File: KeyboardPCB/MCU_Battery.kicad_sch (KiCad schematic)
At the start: 42 parts, among them Q1 CSD17527Q5A, Q2 CSD17527Q5A, U1 ATmega32U4-M, U2 TPS61236PRWLT, U3 BQ24193RGER, U4 BQ297xy, Y1 ECS-160-7-33B-CKL-TR

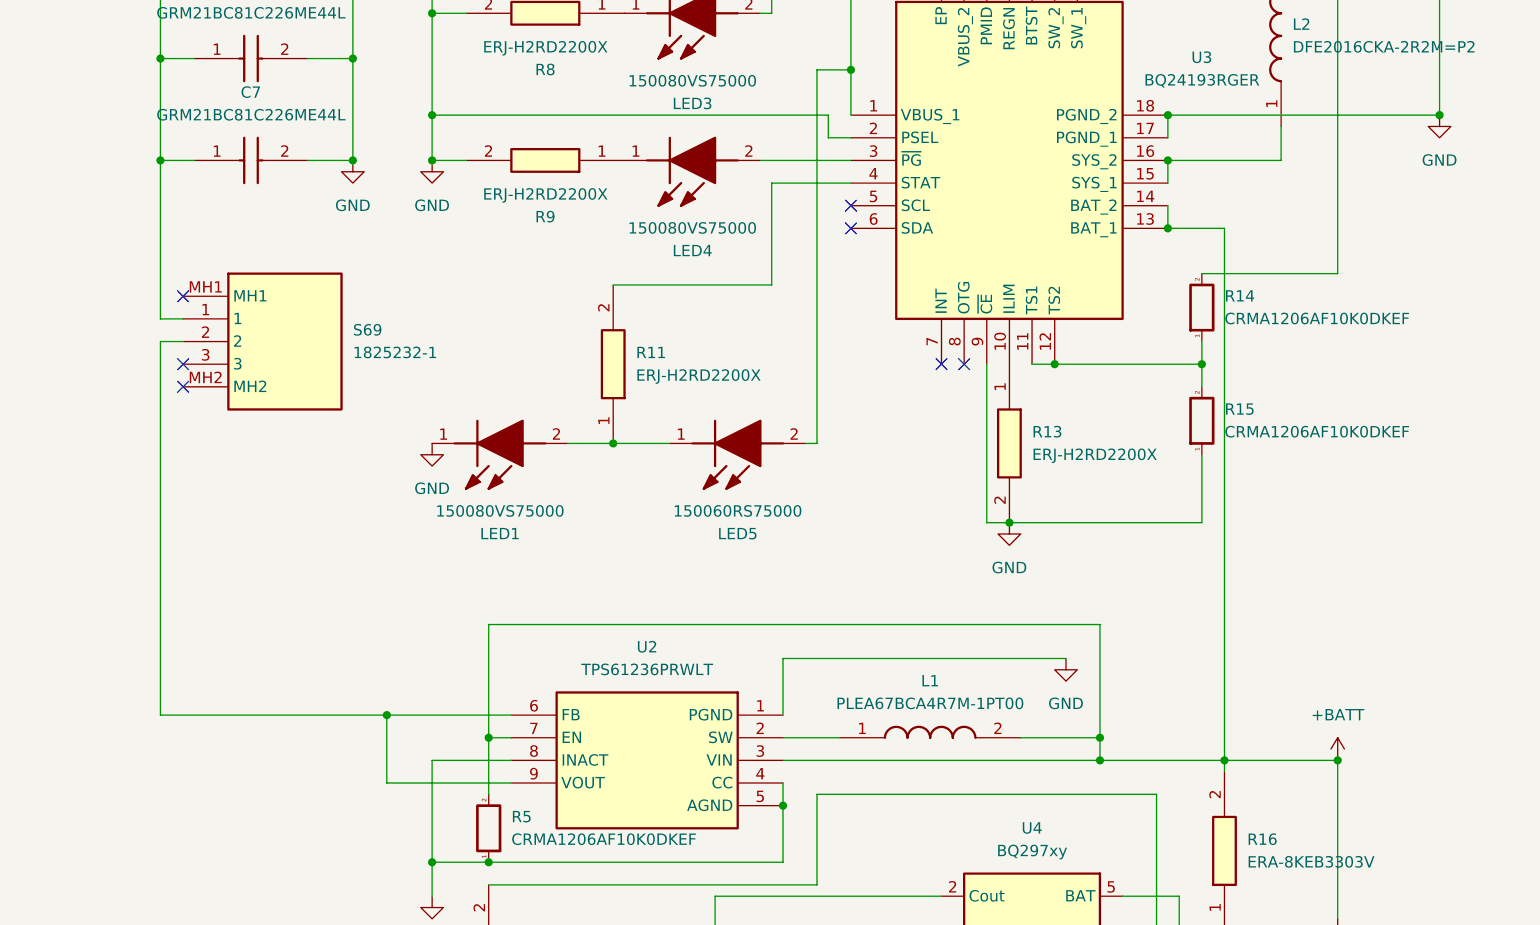
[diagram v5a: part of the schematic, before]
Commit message: Changed location of switch
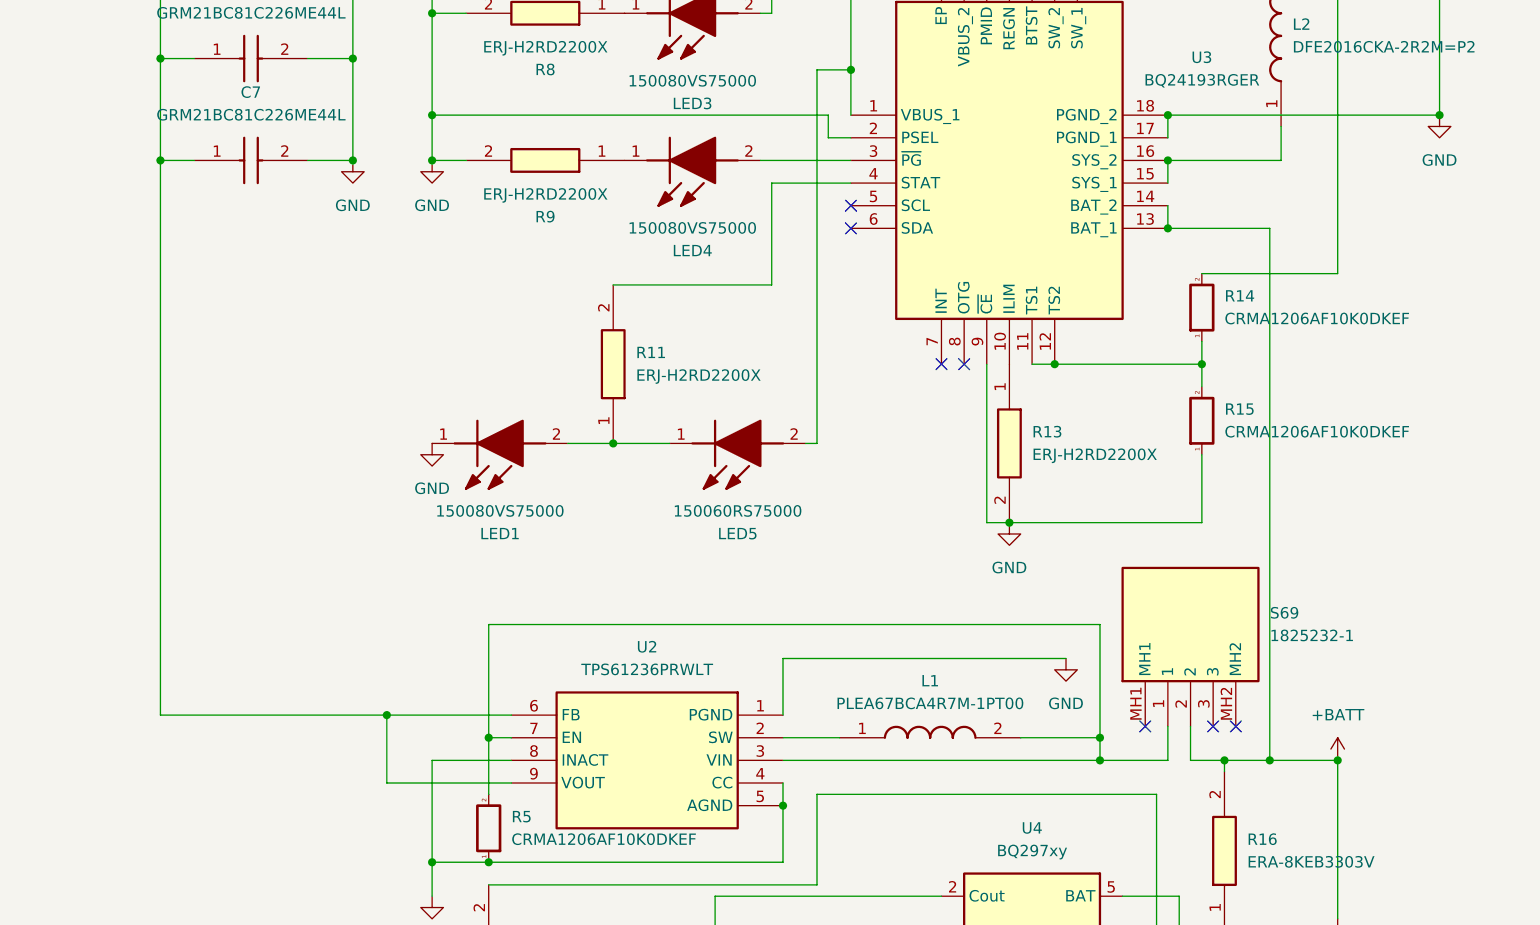
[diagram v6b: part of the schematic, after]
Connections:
- net +BATT: now also S69.2; no longer L1.2, R5.2, U2.3 (VIN), U2.7 (EN)
- net VBUSOUT: now also U2.6 (FB), U2.9 (VOUT); no longer S69.1
- new net: L1.2, R5.2, S69.1, U2.3 (VIN), U2.7 (EN)
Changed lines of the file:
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@@
   (junction (at 73.66 15.24) (diameter 0) (color 0 0 0 0)
   )
+  (junction (at 248.92 118.11) (diameter 0) (color 0 0 0 0)
+  )
+  (junction (at 254 118.11) (diameter 0) (color 0 0 0 0)
+  )
+  (junction (at 229.87 73.66) (diameter 0) (color 0 0 0 0)
+  )
+  (junction (at 160.02 45.72) (diameter 0) (color 0 0 0 0)
+  )
+  (junction (at 55.88 15.24) (diameter 0) (color 0 0 0 0)
+  )
+  (junction (at 166.37 115.57) (diameter 0) (color 0 0 0 0)
+  )
+  (junction (at 261.62 152.4) (diameter 0) (color 0 0 0 0)
+  )
+  (junction (at 160.02 50.8) (diameter 0) (color 0 0 0 0)
+  )
+  (junction (at 40.64 41.91) (diameter 0) (color 0 0 0 0)
+  )
+  (junction (at 250.19 20.32) (diameter 0) (color 0 0 0 0)
+  )
+  (junction (at 55.88 36.83) (diameter 0) (color 0 0 0 0)
+  )
+  (junction (at 242.57 45.72) (diameter 0) (color 0 0 0 0)
+  )
+  (junction (at 219.71 15.24) (diameter 0) (color 0 0 0 0)
+  )
+  (junction (at 255.27 152.4) (diameter 0) (color 0 0 0 0)
+  )
+  (junction (at 129.54 39.37) (diameter 0) (color 0 0 0 0)
+  )
+  (junction (at 261.62 118.11) (diameter 0) (color 0 0 0 0)
+  )
+  (junction (at 179.07 157.48) (diameter 0) (color 0 0 0 0)
+  )
+  (junction (at 217.17 138.43) (diameter 0) (color 0 0 0 0)
+  )
+  (junction (at 209.55 157.48) (diameter 0) (color 0 0 0 0)
+  )
+  (junction (at 248.92 139.7) (diameter 0) (color 0 0 0 0)
+  )
+  (junction (at 129.54 27.94) (diameter 0) (color 0 0 0 0)
+  )
   (junction (at 234.95 118.11) (diameter 0) (color 0 0 0 0)
   )
-  (junction (at 229.87 73.66) (diameter 0) (color 0 0 0 0)
-  )
-  (junction (at 160.02 45.72) (diameter 0) (color 0 0 0 0)
-  )
-  (junction (at 55.88 15.24) (diameter 0) (color 0 0 0 0)
-  )
-  (junction (at 166.37 115.57) (diameter 0) (color 0 0 0 0)
-  )
-  (junction (at 248.92 118.11) (diameter 0) (color 0 0 0 0)
-  )
-  (junction (at 261.62 152.4) (diameter 0) (color 0 0 0 0)
-  )
-  (junction (at 160.02 50.8) (diameter 0) (color 0 0 0 0)
-  )
-  (junction (at 40.64 41.91) (diameter 0) (color 0 0 0 0)
-  )
-  (junction (at 250.19 20.32) (diameter 0) (color 0 0 0 0)
-  )
-  (junction (at 55.88 36.83) (diameter 0) (color 0 0 0 0)
-  )
-  (junction (at 242.57 45.72) (diameter 0) (color 0 0 0 0)
-  )
-  (junction (at 219.71 15.24) (diameter 0) (color 0 0 0 0)
-  )
-  (junction (at 255.27 152.4) (diameter 0) (color 0 0 0 0)
-  )
-  (junction (at 129.54 39.37) (diameter 0) (color 0 0 0 0)
-  )
-  (junction (at 261.62 118.11) (diameter 0) (color 0 0 0 0)
-  )
-  (junction (at 179.07 157.48) (diameter 0) (color 0 0 0 0)
-  )
-  (junction (at 217.17 138.43) (diameter 0) (color 0 0 0 0)
-  )
-  (junction (at 209.55 157.48) (diameter 0) (color 0 0 0 0)
-  )
-  (junction (at 248.92 139.7) (diameter 0) (color 0 0 0 0)
-  )
-  (junction (at 129.54 27.94) (diameter 0) (color 0 0 0 0)
-  )
   (junction (at 273.05 45.72) (diameter 0) (color 0 0 0 0)
   )
@@
   (junction (at 166.37 129.54) (diameter 0) (color 0 0 0 0)
   )
-  (no_connect (at 132.08 76.2))
   (no_connect (at 58.42 52.07))
-  (no_connect (at 132.08 66.04))
+  (no_connect (at 250.19 114.3))
   (no_connect (at 207.01 55.88))
   (no_connect (at 217.17 73.66))
-  (no_connect (at 132.08 73.66))
   (no_connect (at 207.01 58.42))
   (no_connect (at 38.1 27.94))
   (no_connect (at 58.42 57.15))
   (no_connect (at 219.71 73.66))
+  (no_connect (at 240.03 114.3))
+  (no_connect (at 247.65 114.3))
   (wire (pts (xy 196.85 34.29) (xy 198.12 34.29))
     (stroke (width 0) (type default))
@@
     (stroke (width 0) (type default))
   )
-  (wire (pts (xy 129.54 68.58) (xy 129.54 50.8))
+  (wire (pts (xy 129.54 50.8) (xy 129.54 113.03))
     (stroke (width 0) (type default))
   )
@@
     (stroke (width 0) (type default))
   )
-  (wire (pts (xy 129.54 113.03) (xy 129.54 71.12))
-    (stroke (width 0) (type default))
-  )
-  (wire (pts (xy 248.92 58.42) (xy 242.57 58.42))
+  (wire (pts (xy 254 58.42) (xy 242.57 58.42))
     (stroke (width 0) (type default))
   )
@@
     (stroke (width 0) (type default))
   )
+  (wire (pts (xy 248.92 118.11) (xy 245.11 118.11))
+    (stroke (width 0) (type default))
+  )
   (wire (pts (xy 38.1 54.61) (xy 43.18 54.61))
     (stroke (width 0) (type default))
@@
     (stroke (width 0) (type default))
   )
+  (wire (pts (xy 242.57 114.3) (xy 242.57 118.11))
+    (stroke (width 0) (type default))
+  )
   (wire (pts (xy 273.05 19.05) (xy 273.05 45.72))
     (stroke (width 0) (type default))
@@
     (stroke (width 0) (type default))
   )
-  (wire (pts (xy 129.54 71.12) (xy 132.08 71.12))
-    (stroke (width 0) (type default))
-  )
   (wire (pts (xy 180.34 82.55) (xy 186.69 82.55))
     (stroke (width 0) (type default))
@@
     (stroke (width 0) (type default))
   )
-  (wire (pts (xy 132.08 68.58) (xy 129.54 68.58))
-    (stroke (width 0) (type default))
-  )
   (wire (pts (xy 199.39 118.11) (xy 234.95 118.11))
     (stroke (width 0) (type default))
@@
     (stroke (width 0) (type default))
   )
+  (wire (pts (xy 242.57 118.11) (xy 234.95 118.11))
+    (stroke (width 0) (type default))
+  )
   (wire (pts (xy 71.12 24.13) (xy 73.66 24.13))
     (stroke (width 0) (type default))
@@
     (stroke (width 0) (type default))
   )
+  (wire (pts (xy 254 118.11) (xy 248.92 118.11))
+    (stroke (width 0) (type default))
+  )
   (wire (pts (xy 73.66 24.13) (xy 76.2 24.13))
     (stroke (width 0) (type default))
@@
     (stroke (width 0) (type default))
   )
+  (wire (pts (xy 245.11 118.11) (xy 245.11 114.3))
+    (stroke (width 0) (type default))
+  )
   (wire (pts (xy 34.29 68.58) (xy 34.29 64.77))
     (stroke (width 0) (type default))
@@
     (stroke (width 0) (type default))
   )
-  (wire (pts (xy 248.92 118.11) (xy 248.92 58.42))
+  (wire (pts (xy 254 118.11) (xy 254 58.42))
     (stroke (width 0) (type default))
   )
@@
     (stroke (width 0) (type default))
   )
-  (wire (pts (xy 261.62 118.11) (xy 248.92 118.11))
+  (wire (pts (xy 261.62 118.11) (xy 254 118.11))
     (stroke (width 0) (type default))
   )
@@
   )
   (wire (pts (xy 54.61 62.23) (xy 54.61 59.69))
-    (stroke (width 0) (type default))
-  )
-  (wire (pts (xy 234.95 118.11) (xy 248.92 118.11))
     (stroke (width 0) (type default))
   )
@@
     )
   )
-  (symbol (lib_id "keyboard_syms:1825232-1") (at 143.51 69.85 0) (unit 1)
+  (symbol (lib_id "keyboard_syms:1825232-1") (at 243.84 102.87 90) (unit 1)
     (in_bom yes) (on_board yes) (dnp no) (fields_autoplaced)
-    (property "Reference" "S69" (at 151.13 69.85 0)
-      (effects (font (size 1.27 1.27)) (justify left))
-    )
-    (property "Value" "1825232-1" (at 151.13 72.39 0)
-      (effects (font (size 1.27 1.27)) (justify left))
-    )
-    (property "Footprint" "keyboard_syms:18252321" (at 162.56 164.77 0)
-      (effects (font (size 1.27 1.27)) (justify left top) hide)
-    )
-    (property "Datasheet" "https://componentsearchengine.com/Datasheets/1/1825232-1.pdf" (at 162.56 264.77 0)
-      (effects (font (size 1.27 1.27)) (justify left top) hide)
-    )
-    (property "Height" "3.7" (at 162.56 464.77 0)
-      (effects (font (size 1.27 1.27)) (justify left top) hide)
-    )
-    (property "Manufacturer_Name" "TE Connectivity" (at 162.56 564.77 0)
-      (effects (font (size 1.27 1.27)) (justify left top) hide)
-    )
-    (property "Manufacturer_Part_Number" "1825232-1" (at 162.56 664.77 0)
-      (effects (font (size 1.27 1.27)) (justify left top) hide)
-    )
-    (property "Mouser Part Number" "655-1825232-1" (at 162.56 764.77 0)
-      (effects (font (size 1.27 1.27)) (justify left top) hide)
-    )
-    (property "Mouser Price/Stock" "https://www.mouser.co.uk/ProductDetail/TE-Connectivity-PB/1825232-1?qs=kTKVN3NWb5FosGxaNC1%252BtA%3D%3D" (at 162.56 864.77 0)
-      (effects (font (size 1.27 1.27)) (justify left top) hide)
-    )
-    (property "Arrow Part Number" "1825232-1" (at 162.56 964.77 0)
-      (effects (font (size 1.27 1.27)) (justify left top) hide)
-    )
-    (property "Arrow Price/Stock" "https://www.arrow.com/en/products/1825232-1/te-connectivity?region=europe" (at 162.56 1064.77 0)
-      (effects (font (size 1.27 1.27)) (justify left top) hide)
-    )
+    (property "Reference" "S69" (at 254 101.6 90)
+      (effects (font (size 1.27 1.27)) (justify right))
+    )
+    (property "Value" "1825232-1" (at 254 104.14 90)
+      (effects (font (size 1.27 1.27)) (justify right))
+    )
+    (property "Footprint" "keyboard_syms:18252321" (at 338.76 83.82 0)
+      (effects (font (size 1.27 1.27)) (justify left top) hide)
+    )
+    (property "Datasheet" "https://componentsearchengine.com/Datasheets/1/1825232-1.pdf" (at 438.76 83.82 0)
+      (effects (font (size 1.27 1.27)) (justify left top) hide)
+    )
+    (property "Height" "3.7" (at 638.76 83.82 0)
+      (effects (font (size 1.27 1.27)) (justify left top) hide)
+    )
+    (property "Manufacturer_Name" "TE Connectivity" (at 738.76 83.82 0)
+      (effects (font (size 1.27 1.27)) (justify left top) hide)
+    )
+    (property "Manufacturer_Part_Number" "1825232-1" (at 838.76 83.82 0)
+      (effects (font (size 1.27 1.27)) (justify left top) hide)
+    )
+    (property "Mouser Part Number" "655-1825232-1" (at 938.76 83.82 0)
+      (effects (font (size 1.27 1.27)) (justify left top) hide)
+    )
+    (property "Mouser Price/Stock" "https://www.mouser.co.uk/ProductDetail/TE-Connectivity-PB/1825232-1?qs=kTKVN3NWb5FosGxaNC1%252BtA%3D%3D" (at 1038.76 83.82 0)
+      (effects (font (size 1.27 1.27)) (justify left top) hide)
+    )
+    (property "Arrow Part Number" "1825232-1" (at 1138.76 83.82 0)
+      (effects (font (size 1.27 1.27)) (justify left top) hide)
+    )
+    (property "Arrow Price/Stock" "https://www.arrow.com/en/products/1825232-1/te-connectivity?region=europe" (at 1238.76 83.82 0)
+      (effects (font (size 1.27 1.27)) (justify left top) hide)
+    )
